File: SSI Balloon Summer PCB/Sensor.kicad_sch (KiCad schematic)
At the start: 0 parts

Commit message: Finished sensors + tidied up schematic
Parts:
- added C11: 0.1uF, symbol Device:C
- added C12: 2.2uF, symbol Device:C
- added C42, C45: 10nF, symbol Device:C
- added C43, C44, C46: 100nF, symbol Device:C
- added J8: PT1000 Sensor, symbol Connector_Generic:Conn_01x03
- added R21: 4300, symbol Device:R
- added R22: 10M, symbol Device:R
- added U10: MS5611-01BA03, MS5611-01BA03:SON125P500X300X100-8N, symbol MS5611-01BA03:MS5611-01BA03
- added U4: ICM-42688-P, ICM-42688-P:PQFN50P300X250X97-14N, symbol ICM-42688-P:ICM-42688-P
- added U9: MAX31865ATP_T, MAX31865ATP_T:QFN65P500X500X80-21N, symbol MAX31865ATP_T:MAX31865ATP_T
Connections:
- new net: R21.1, U9.3 (REFIN-), U9.4 (ISENSOR)
- new net: J8.1 (Pin_1), U9.5 (FORCE+), U9.6 (FORCE2)
- new net: C45.1, J8.2 (Pin_2), R22.1, U9.7 (RTDIN+)
- new net: C45.2, J8.3 (Pin_3), U9.8 (RTDIN-), U9.9 (FORCE-)
- new net +3V3: C11.2, C12.2, C42.1, C43.2, C44.1, C46.2, U10.1 (VDD), U4.5 (VDDIO), U4.8 (VDD), U9.19 (DVDD), U9.20 (VDD)
- new net BARO_CS: U10.4 (CSB), U10.5 (CSB)
- new net BIAS: R21.2, R22.2, U9.1 (BIAS), U9.2 (REFIN+)
- new net GND: C11.1, C12.1, C42.2, C43.1, C44.2, C46.1, U10.2 (PS), U10.3 (GND), U4.6 (GND), U4.7 (RESV_7), U4.9 (INT2/FSYNC/CLKIN), U9.10 (GND2), U9.15 (DGND), U9.16 (GND1), U9.21 (EP)
- new net IMU_CS: U4.12 (AP_CS)
- new net IMU_INT1: U4.4 (INT1/INT)
- new net MISO: U10.6 (SDO), U4.1 (AP_SDO/AP_AD0), U9.14 (SDO)
- new net MOSI: U10.7 (SDI/SDA), U4.14 (AP_SDA/AP_SDIO/AP_SDI), U9.11 (SDI)
- new net SCK: U10.8 (SCLK), U4.13 (AP_SCL/AP_SCLK), U9.12 (SCLK)
- new net Temp_CS: U9.13 (~{CS})
- no-connect marks 0 -> 4
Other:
- note added: "Input:"
- note added: "Output:"
- note added: "Passive:"

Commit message: stuff
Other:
- note added: "understand left side of temp sensor"
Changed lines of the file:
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@@
+		)
+	)
+	(text "understand left side of temp sensor\n"
+		(exclude_from_sim no)
+		(at 154.94 63.246 0)
+		(effects
+			(font
+				(size 1.27 1.27)
+			)
 		)
 	)

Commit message: Fixed I2C and SPI issues
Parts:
- added R23, R24, R25: 10k, symbol Device:R
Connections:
- net +3V3: now also R23.1, R24.1, R25.1
- net BARO_CS: now also R25.2
- net IMU_CS: now also R24.2
- net Temp_CS: now also R23.2

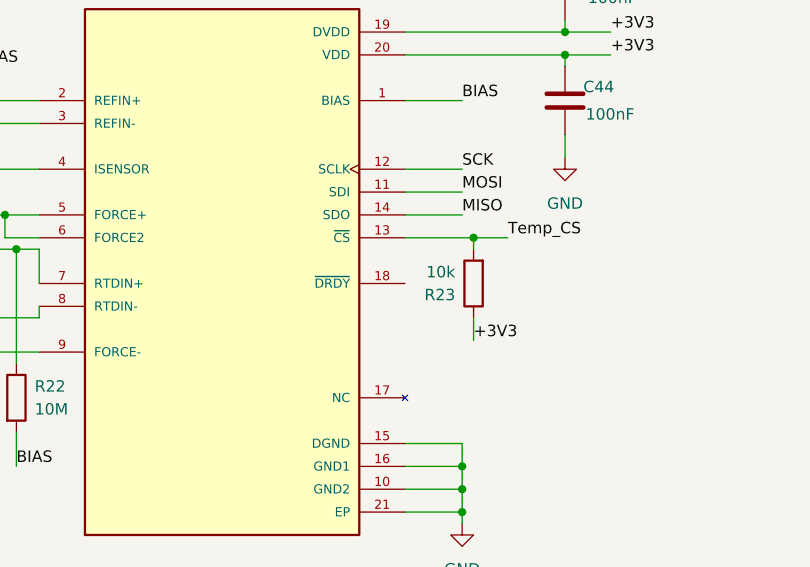
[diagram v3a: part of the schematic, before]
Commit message: Fixed ERC - no ERC errors
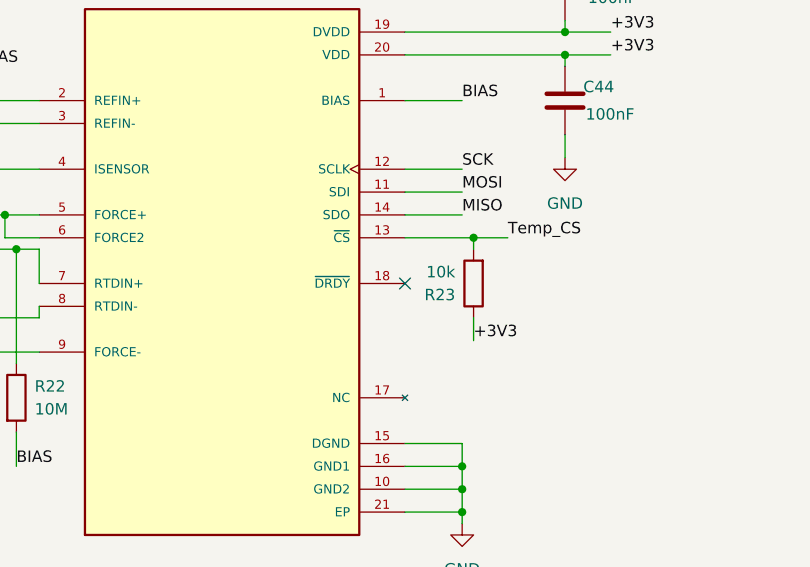
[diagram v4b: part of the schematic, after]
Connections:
- no-connect marks 4 -> 5
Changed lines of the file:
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@@
+	)
+	(no_connect
+		(at 210.82 97.79)
 	)
 	(no_connect

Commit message: Overhauled power symbols for consistency and ERC
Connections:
- net +3V3: now also C43.1, R25.2; no longer C43.2, R25.1
- net BARO_CS: now also R25.1; no longer R25.2
- net GND: now also C43.2; no longer C43.1
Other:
- note removed: "Passive:"
- moved on the sheet: C43, C44, R23, R25

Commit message: fixed footprints
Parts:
- C11, C12, C42, C43, C44, C45, C46: footprint (none) -> Capacitor_SMD:C_0603_1608Metric
- J8: footprint (none) -> Connector_JST:JST_PH_B3B-PH-K_1x03_P2.00mm_Vertical
- R21, R22, R23, R24, R25: footprint (none) -> Resistor_SMD:R_0603_1608Metric
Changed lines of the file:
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@@
 			)
 		)
-		(property "Footprint" ""
+		(property "Footprint" "Resistor_SMD:R_0603_1608Metric"
 			(at 226.822 87.63 90)
 			(hide yes)
@@
 			)
 		)
-		(property "Footprint" ""
+		(property "Footprint" "Resistor_SMD:R_0603_1608Metric"
 			(at 37.338 101.6 90)
 			(hide yes)
@@
 			)
 		)
-		(property "Footprint" ""
+		(property "Footprint" "Resistor_SMD:R_0603_1608Metric"
 			(at 153.67 79.248 90)
 			(hide yes)
@@
 			)
 		)
-		(property "Footprint" ""
+		(property "Footprint" "Capacitor_SMD:C_0603_1608Metric"
 			(at 116.5352 81.28 0)
 			(hide yes)
@@
 			)
 		)
-		(property "Footprint" ""
+		(property "Footprint" "Capacitor_SMD:C_0603_1608Metric"
 			(at 105.1052 81.28 0)
 			(hide yes)
@@
 			)
 		)
-		(property "Footprint" ""
+		(property "Footprint" "Resistor_SMD:R_0603_1608Metric"
 			(at 79.248 147.32 90)
 			(hide yes)
@@
 			)
 		)
-		(property "Footprint" ""
+		(property "Footprint" "Resistor_SMD:R_0603_1608Metric"
 			(at 165.862 110.49 90)
 			(hide yes)
@@
 			)
 		)
-		(property "Footprint" ""
+		(property "Footprint" "Capacitor_SMD:C_0603_1608Metric"
 			(at 152.0952 140.97 0)
 			(hide yes)
@@
 			)
 		)
-		(property "Footprint" ""
+		(property "Footprint" "Capacitor_SMD:C_0603_1608Metric"
 			(at 225.7552 60.96 0)
 			(hide yes)
@@
 			)
 		)
-		(property "Footprint" ""
+		(property "Footprint" "Capacitor_SMD:C_0603_1608Metric"
 			(at 159.7152 101.6 0)
 			(hide yes)
@@
 			)
 		)
-		(property "Footprint" ""
+		(property "Footprint" "Capacitor_SMD:C_0603_1608Metric"
 			(at 252.4252 81.28 0)
 			(hide yes)
@@
 			)
 		)
-		(property "Footprint" ""
+		(property "Footprint" "Capacitor_SMD:C_0603_1608Metric"
 			(at 124.1552 95.25 0)
 			(hide yes)
@@
 			)
 		)
-		(property "Footprint" ""
+		(property "Footprint" "Connector_JST:JST_PH_B3B-PH-K_1x03_P2.00mm_Vertical"
 			(at 151.13 92.71 0)
 			(hide yes)

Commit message: Edits to PCB placement + traces - RF and GPS next
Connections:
- net +3V3: now also R25.1; no longer R25.2
- net BARO_CS: now also R25.2; no longer R25.1
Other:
- moved on the sheet: R25
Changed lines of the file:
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@@
+	)
+	(junction
+		(at 77.47 151.13)
+		(diameter 0)
+		(color 0 0 0 0)
 	)
 	(junction
@@
 	)
 	(junction
-		(at 77.47 151.13)
-		(diameter 0)
-		(color 0 0 0 0)
-	)
-	(junction
 		(at 123.19 86.36)
 		(diameter 0)
@@
 	(wire
 		(pts
+			(xy 77.47 151.13) (xy 111.76 151.13)
+		)
+		(stroke
+			(width 0)
+			(type default)
+		)
+	)
+	(wire
+		(pts
 			(xy 210.82 87.63) (xy 217.17 87.63)
 		)
@@
 		(pts
 			(xy 35.56 96.52) (xy 35.56 97.79)
-		)
-		(stroke
-			(width 0)
-			(type default)
-		)
-	)
-	(wire
-		(pts
-			(xy 77.47 151.13) (xy 111.76 151.13)
 		)
 		(stroke
@@
 	(symbol
 		(lib_id "Device:R")
-		(at 77.47 147.32 180)
+		(at 77.47 147.32 0)
 		(unit 1)
 		(body_style 1)
@@
 		(dnp no)
 		(property "Reference" "R25"
-			(at 75.438 148.59 0)
+			(at 79.502 146.05 0)
 			(show_name no)
 			(do_not_autoplace no)
@@
 		)
 		(property "Value" "10k"
-			(at 75.438 146.05 0)
+			(at 79.502 148.59 0)
 			(show_name no)
 			(do_not_autoplace no)
@@
 		)
 		(property "Footprint" "Resistor_SMD:R_0603_1608Metric"
-			(at 79.248 147.32 90)
-			(hide yes)
-			(show_name no)
+			(at 75.692 147.32 90)
+			(hide yes)
+			(show_name no)
